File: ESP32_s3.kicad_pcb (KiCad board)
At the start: 2 copper layers, 100 x 80 mm, 72 parts, among them J11 backup, J13 Jetson Power Supply, J13 jetsonnano, J14 TXRX, J15 TXRX2, J3 Conn_01x02, J4 Servo motor, J5 PJ-040DH, J7 Conn_01x02, J8 Conn_01x02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

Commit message: fix net label
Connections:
- net /GPIO13 renamed GPIO13
- C4 pad 1: 5V -> +5V
- Cin1 pad 1: 5V -> +5V
- Cin2 pad 1: 5V -> +5V
- D10 pad 1: 5V -> +5V
- J13 pad 1: 5V -> +5V
- J13 pad 2: 5V -> +5V
- J4 pad 2: 5V -> +5V
- L1 pad 1: 5V -> +5V
- R11 pad 1: 5V -> +5V
- R15 pad 2: 5V -> +5V
- RbLED1 pad 1: 5V -> +5V
- U2 pad 3: 5V -> +5V
- U3 pad 9: 5V -> +5V
- U4 pad 9: 5V -> +5V
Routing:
- net 5V: track 91.1 -> 0.00 mm, vias 4 -> 0
- net +5V: track 88.6 -> 179.7 mm, vias 0 -> 4
- added copper zone on F.Cu, net +5V
- removed copper zone on F.Cu, net 5V

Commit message: update traces
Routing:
- net +5V: track 179.7 -> 205.0 mm, vias 4 -> 5
- net 3.3V: track 141.4 -> 149.4 mm
- net GND: track 381.4 -> 382.2 mm

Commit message: change layout
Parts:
- moved J4 66.1 mm to (133.2, 114.8)
- moved J13 65.8 mm to (133.5, 120.5)
- moved J8 64.0 mm to (163.2, 128.0)
- moved J7 60.1 mm to (132.0, 128.8)
- moved J9 59.9 mm to (153.1, 128.3), turned to 0 degrees
- moved J3 59.6 mm to (143.8, 128.5)
- moved Cbst1 50.9 mm to (155.7, 67.9)
- moved Ccomp2 50.9 mm to (170.2, 62.9)
- moved Cin1 50.9 mm to (144.2, 72.3)
- moved Cin2 50.9 mm to (148.2, 72.0)
- moved Cout1 50.9 mm to (164.2, 70.5)
- moved Css1 50.9 mm to (157.7, 73.5)
- moved Cvcc1 50.9 mm to (155.7, 59.5)
- moved DbLED1 50.9 mm to (151.7, 76.5)
- moved DrLED1 50.9 mm to (168.0, 71.0)
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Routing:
- net GND: track 382.2 -> 27.7 mm, vias 11 -> 0
- net +5V: track 205.0 -> 0.00 mm, vias 5 -> 0
- net 3.3V: track 149.4 -> 12.0 mm, vias 4 -> 0
- net 8V: track 100.8 -> 0.00 mm, vias 2 -> 0
- net GPIO13: track 72.7 -> 0.00 mm, vias 2 -> 0
- net Net-(D2-A): track 72.1 -> 0.00 mm
- net Net-(D8-A): track 59.1 -> 0.00 mm
- net GPIO9: track 59.0 -> 0.00 mm
- net /EN: track 63.4 -> 5.28 mm
- net GPIO10: track 57.7 -> 0.00 mm
- net Net-(D4-A): track 55.4 -> 0.00 mm
- net GPIO11: track 52.3 -> 0.00 mm, vias 2 -> 0
- net GPIO12: track 51.4 -> 0.00 mm, vias 2 -> 0
- net Net-(D6-A): track 49.6 -> 0.00 mm, vias 1 -> 0
- net /GPIO0: track 42.5 -> 0.00 mm, vias 2 -> 0
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
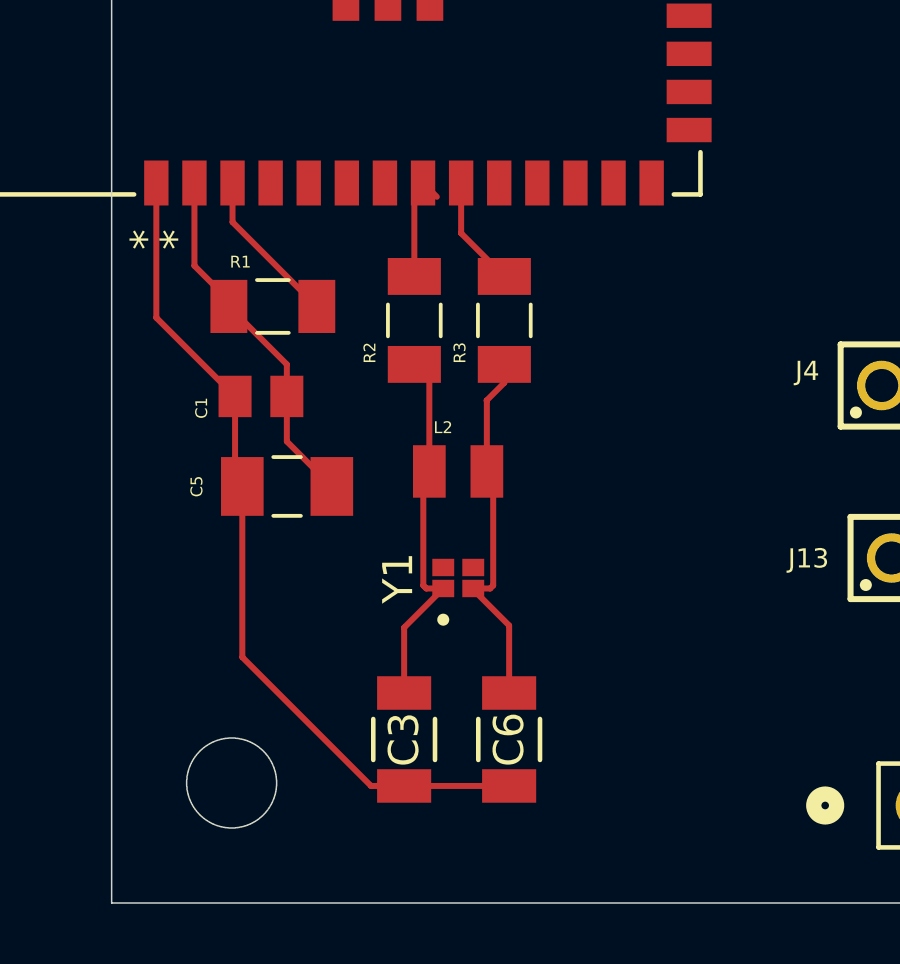
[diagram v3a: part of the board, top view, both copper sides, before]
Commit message: delete 40MHZ crystal oscillator
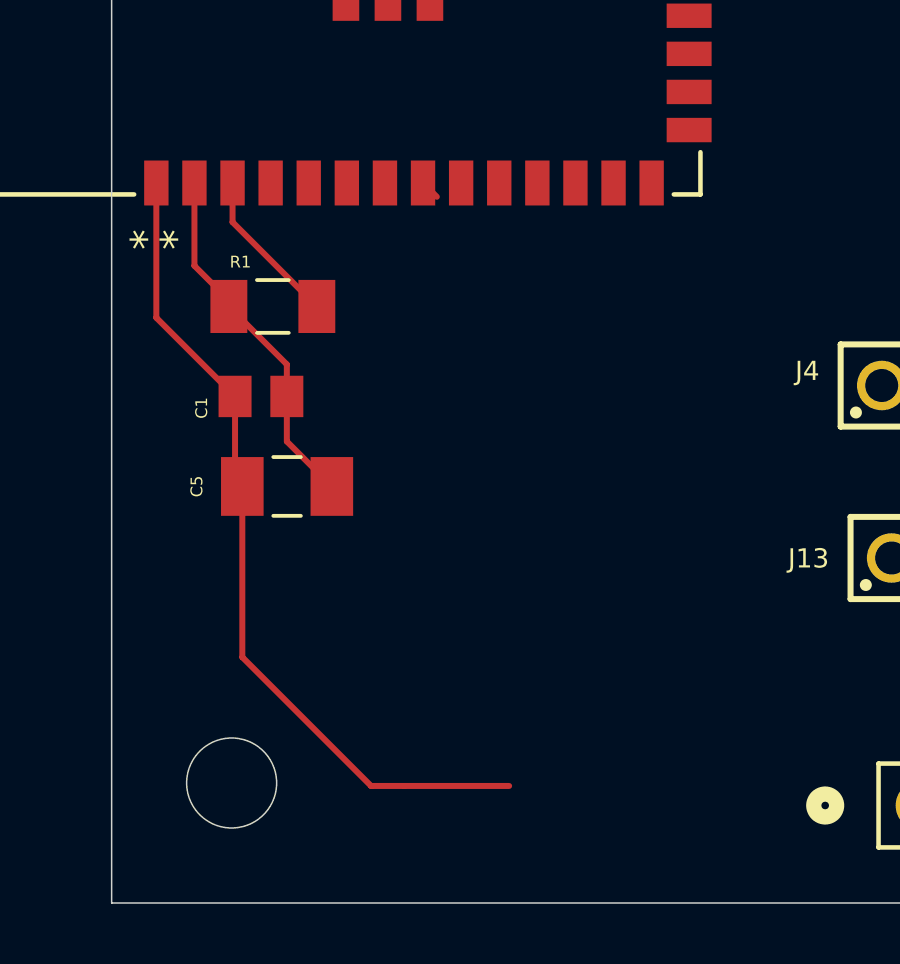
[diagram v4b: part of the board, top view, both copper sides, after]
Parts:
- removed C3, C6: 12pF, CC1206JKNPODBN120:CAP_CC1206_YAG
- removed L2: L, LQW2BAN24NG00L:INDC2015X152N
- removed R2, R3: 0, RMCF1206ZR0R00:RESC3216X70N
- removed Y1: Crystal, crystal:XTAL_ABM12W-40.0000MHZ-6-B1U-T3
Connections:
- U1 pad 8: Net-(U1-IO15) -> unconnected-(U1-IO15-Pad8)
- U1 pad 9: Net-(U1-IO16) -> unconnected-(U1-IO16-Pad9)
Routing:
- net Net-(C6-Pad2): track 12.4 -> 0.00 mm
- net Net-(C3-Pad2): track 12.4 -> 0.00 mm
- net Net-(U1-IO15): track 3.89 -> 0.00 mm
- net Net-(U1-IO16): track 3.71 -> 0.00 mm
- net unconnected-(U1-IO15-Pad8): track 0.00 -> 1.06 mm

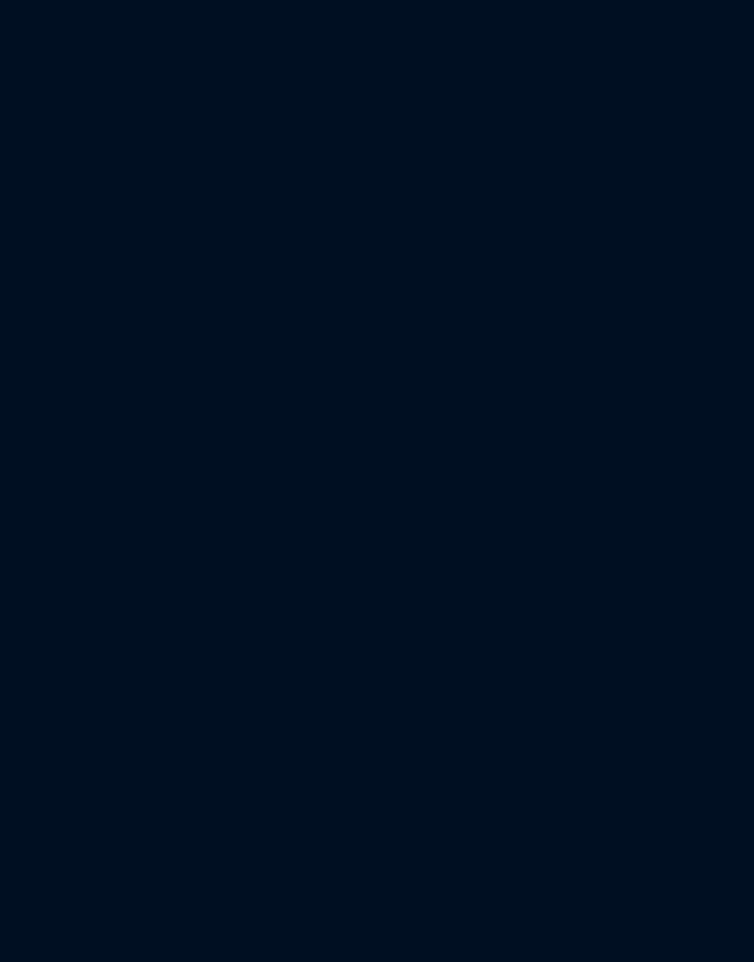
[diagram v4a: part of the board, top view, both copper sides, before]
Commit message: footprint fix
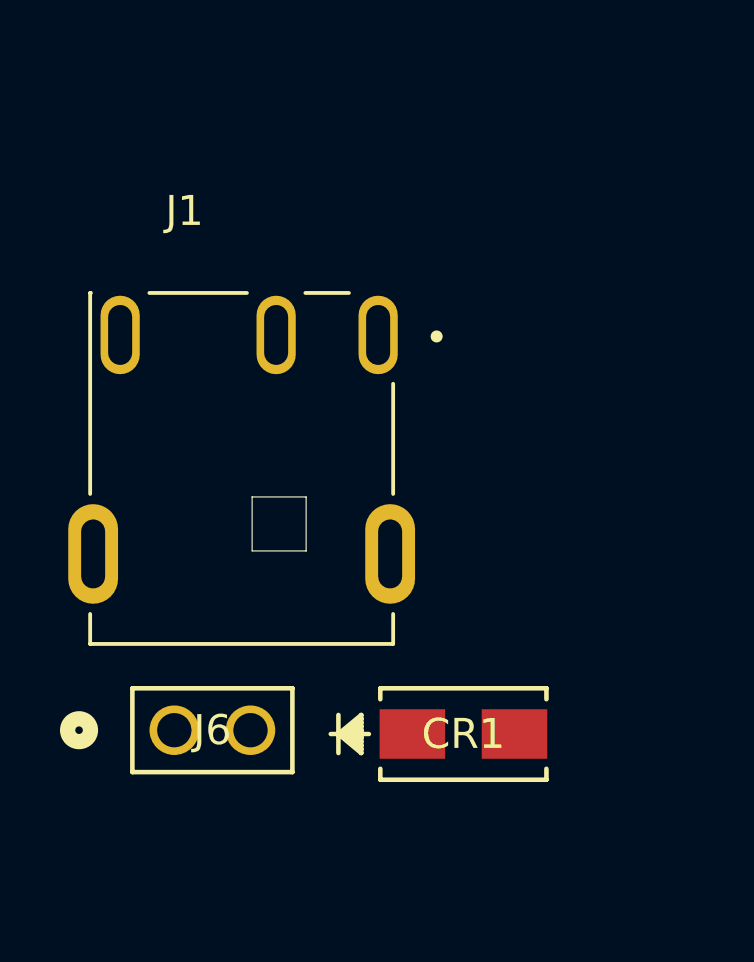
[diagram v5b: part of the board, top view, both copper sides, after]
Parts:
- added CR1: SMAJ10A, SMAJ10A:SMASeries_LTF, F.Cu at (78.8, 101.5)
- added J1: 54-00127, 54-00127:TENSILITY_54-00127, F.Cu at (71.4, 95.5)
- added J6: jetson nano, 01x02connector:CONN_61300211121_WRE, F.Cu at (69.2, 101.4)

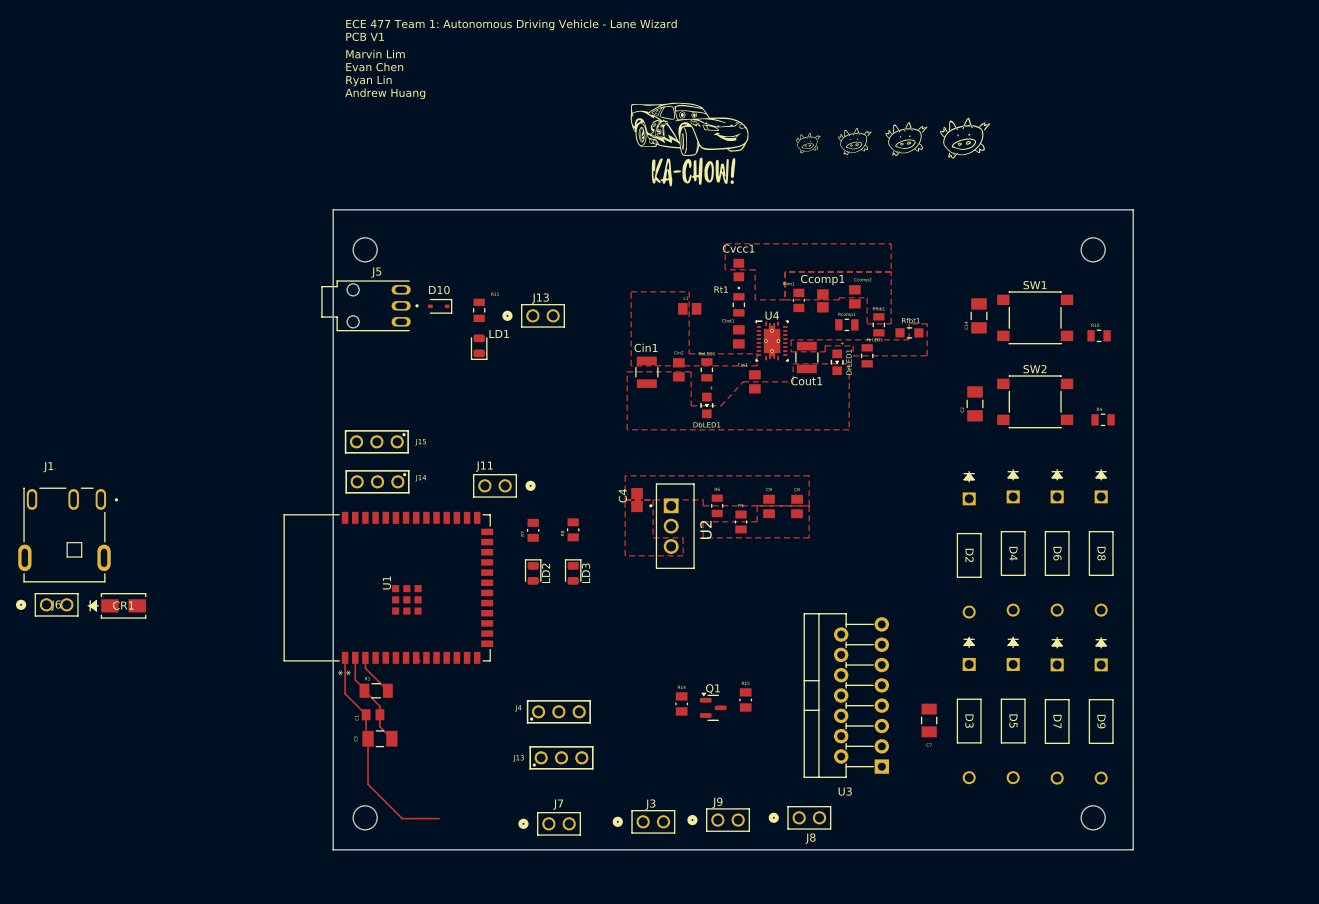
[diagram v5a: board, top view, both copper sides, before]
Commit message: update schematic and layout
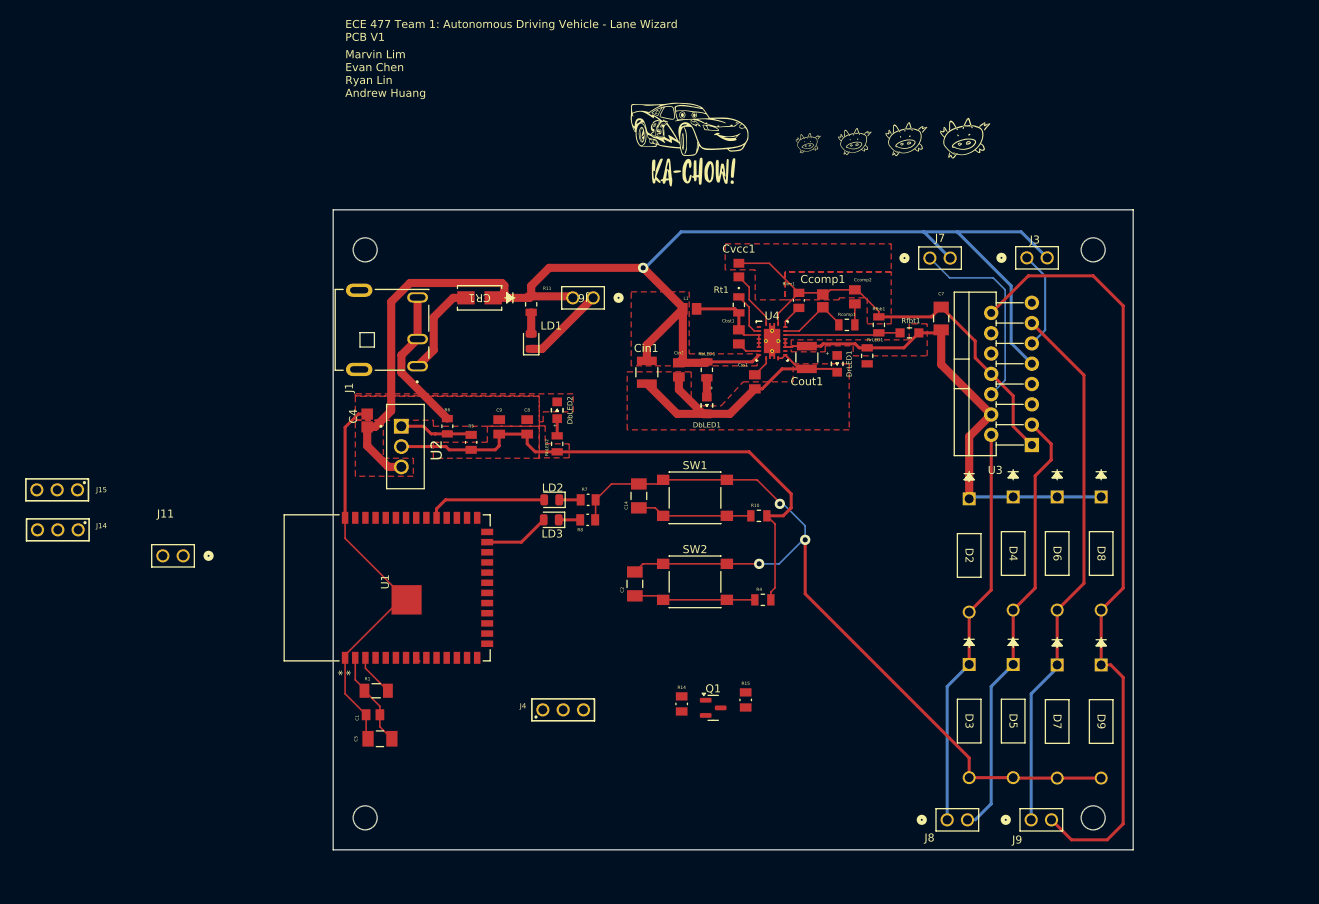
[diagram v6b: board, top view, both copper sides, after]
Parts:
- removed D10: BAT60JFILM, Diode_SMD:D_SOD-323
- removed J13: jetsonnano, 61300311121:61300311121
- removed J13: Jetson Power Supply, 01x02connector:CONN_61300211121_WRE
- removed J5: PJ-040DH, BarrelJack:CUI_PJ-040DH
- added DbLED2: LED blue, WL-SMCW_0805:WL-SMCW_0805, F.Cu at (133.0, 77.0)
- added RbLED2: 250, CRCW080535K7FKEA:RESC2012X50N, F.Cu at (133.0, 81.2)
- moved J3 85.3 mm to (191.7, 58.0)
- moved J7 85.3 mm to (179.6, 58.0)
- moved J6 78.4 mm to (137.5, 63.0), turned to 180 degrees
- moved CR1 58.8 mm to (123.3, 63.0), turned to 180 degrees
- moved C7 50.3 mm to (181.0, 65.6), turned to 90 degrees
- moved SW1 48.1 mm to (150.2, 88.0)
- moved SW2 48.1 mm to (150.2, 98.5)
- moved C14 48.1 mm to (143.2, 87.8)
- moved C2 48.1 mm to (142.7, 98.8)
- moved R10 48.1 mm to (158.2, 90.2)
- moved R4 48.1 mm to (158.7, 100.8)
- moved J1 46.6 mm to (108.2, 67.0), turned to -90 degrees
- moved U3 44.4 mm to (192.3, 81.4)
- moved J11 41.2 mm to (86.2, 95.2)
- moved J14 40.4 mm to (70.6, 92.0)
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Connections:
- J3 pad 2: Net-(J3-Pin_2) -> +5V
- J7 pad 2: Net-(J3-Pin_2) -> +5V
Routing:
- net GND: track 27.7 -> 286.0 mm, vias 0 -> 3
- net +5V: track 0.00 -> 181.1 mm, vias 0 -> 1
- net Net-(D8-A): track 0.00 -> 98.5 mm
- net 3.3V: track 12.0 -> 82.7 mm
- net Net-(D6-A): track 0.00 -> 67.5 mm
- net 8V: track 0.00 -> 63.7 mm
- net Net-(D4-A): track 0.00 -> 54.3 mm
- net Net-(D2-A): track 0.00 -> 50.7 mm
- net Net-(J7-Pin_1): track 0.00 -> 24.8 mm
- net /GPIO0: track 0.00 -> 15.2 mm
- net /GPIO38: track 0.00 -> 15.0 mm
- net Net-(U4-FB): track 0.00 -> 14.5 mm
- net /EN: track 5.28 -> 19.7 mm
- net Net-(J3-Pin_1): track 0.00 -> 12.3 mm
- net Net-(CR1-Pad2): track 0.00 -> 12.0 mm
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
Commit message: update traces
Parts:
- moved J15 64.9 mm to (127.0, 55.0)
- moved J14 60.1 mm to (118.0, 55.0), turned to 0 degrees
- moved J11 36.6 mm to (121.3, 84.8), turned to 0 degrees
- moved C14 35.7 mm to (139.8, 123.3)
- moved R10 35.7 mm to (154.8, 125.8)
- moved SW1 35.7 mm to (146.8, 123.5)
- moved J4 32.7 mm to (142.5, 83.0)
- moved R14 27.3 mm to (137.8, 88.7)
- moved R15 27.3 mm to (145.8, 88.2)
- moved Q1 27.3 mm to (141.7, 89.2)
- moved C2 15.0 mm to (139.0, 113.3)
- moved R4 15.0 mm to (155.0, 115.2)
- moved SW2 15.0 mm to (146.5, 113.0)
- moved LD2 4.56 mm to (127.8, 87.5)
- moved LD3 4.56 mm to (127.8, 90.0)
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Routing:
- net GND: track 286.0 -> 392.8 mm, vias 3 -> 5
- net GPIO10: track 0.00 -> 91.8 mm, vias 0 -> 1
- net GPIO9: track 0.00 -> 87.3 mm, vias 0 -> 1
- net GPIO12: track 0.00 -> 76.5 mm, vias 0 -> 1
- net GPIO11: track 0.00 -> 76.4 mm, vias 0 -> 1
- net 3.3V: track 82.7 -> 132.1 mm, vias 0 -> 6
- net /RXD0: track 0.00 -> 46.6 mm, vias 0 -> 1
- net /GPIO0: track 15.2 -> 61.6 mm, vias 0 -> 2
- net /TXD0: track 0.00 -> 45.6 mm, vias 0 -> 1
- net /GPIO1: track 0.00 -> 45.0 mm, vias 0 -> 1
- net /GPIO2: track 0.00 -> 40.5 mm, vias 0 -> 1
- net /EN: track 19.7 -> 52.8 mm
- net +5V: track 181.1 -> 208.0 mm, vias 1 -> 3
- net GPIO13: track 0.00 -> 23.1 mm
- net /GPIO42: track 0.00 -> 15.6 mm, vias 0 -> 1
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- added copper zone on B.Cu, net GND
